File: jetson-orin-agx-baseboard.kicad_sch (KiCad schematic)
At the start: 0 parts

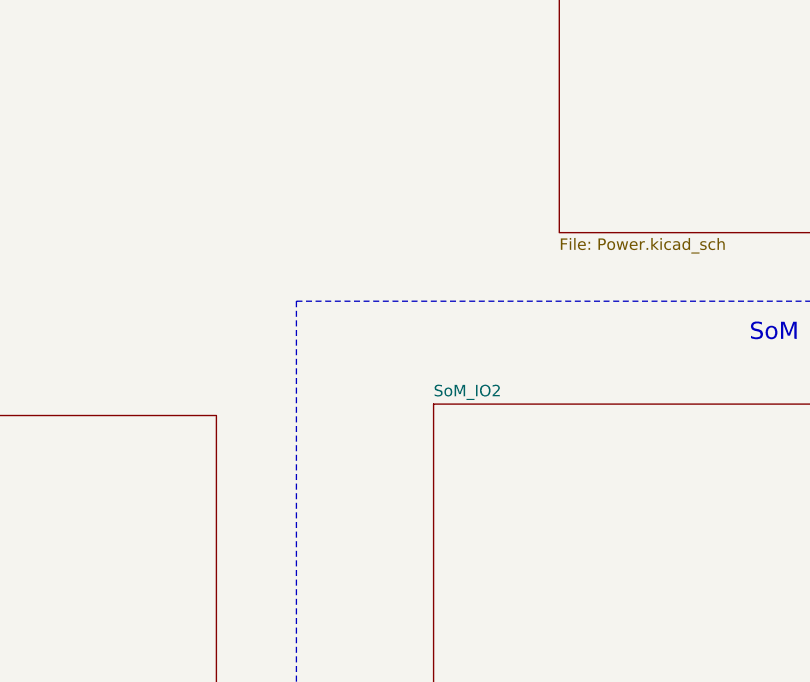
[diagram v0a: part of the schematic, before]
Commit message: [#81782] Add DC section
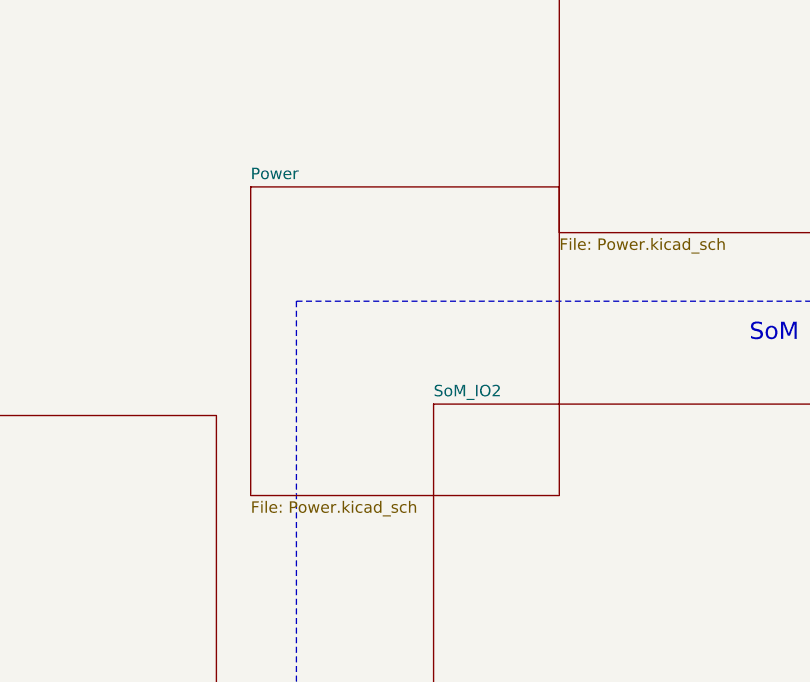
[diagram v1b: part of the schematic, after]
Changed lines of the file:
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@@
+		)
+	)
+	(sheet
+		(at 228.6 119.38)
+		(size 34.29 34.29)
+		(exclude_from_sim no)
+		(in_bom yes)
+		(on_board yes)
+		(dnp no)
+		(fields_autoplaced yes)
+		(stroke
+			(width 0.1524)
+			(type solid)
+		)
+		(fill
+			(color 0 0 0 0.0000)
+		)
+		(property "Sheetname" "Power"
+			(at 228.6 118.6684 0)
+			(effects
+				(font
+					(size 1.27 1.27)
+				)
+				(justify left bottom)
+			)
+		)
+		(property "Sheetfile" "Power.kicad_sch"
+			(at 228.6 154.2546 0)
+			(effects
+				(font
+					(size 1.27 1.27)
+				)
+				(justify left top)
+			)
+		)
+		(instances
+			(project "jetson-orin-agx-baseboard"
+				(path "/f569b0be-0afd-48b7-93ee-28582a4c645c"
+					(page "7")
+				)
+			)
 		)
 	)

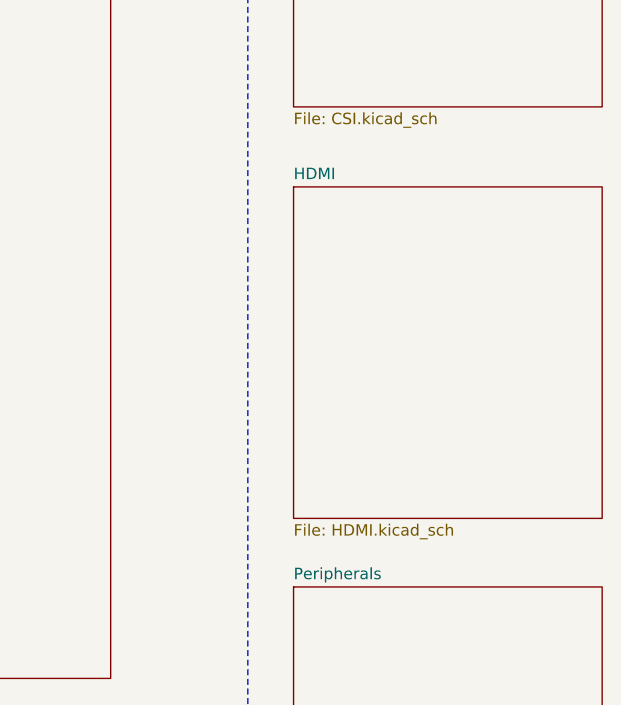
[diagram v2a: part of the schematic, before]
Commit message: [#81970] Add SFP sheet and power section
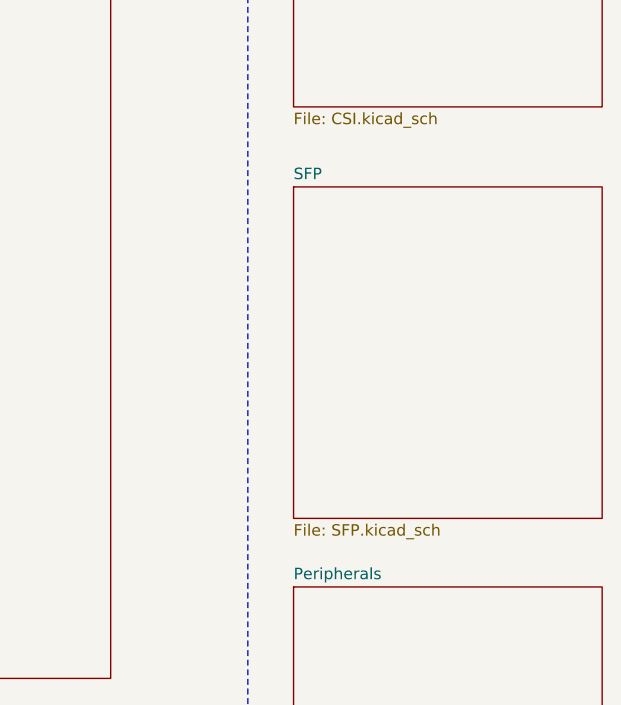
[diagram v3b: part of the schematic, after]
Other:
- sheet HDMI renamed SFP
- sheet SFP: file HDMI.kicad_sch -> SFP.kicad_sch
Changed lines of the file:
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@@
 			(color 0 0 0 0.0000)
 		)
-		(property "Sheetname" "HDMI"
+		(property "Sheetname" "SFP"
 			(at 346.71 235.5084 0)
 			(effects
@@
 			)
 		)
-		(property "Sheetfile" "HDMI.kicad_sch"
+		(property "Sheetfile" "SFP.kicad_sch"
 			(at 346.71 273.6346 0)
 			(effects

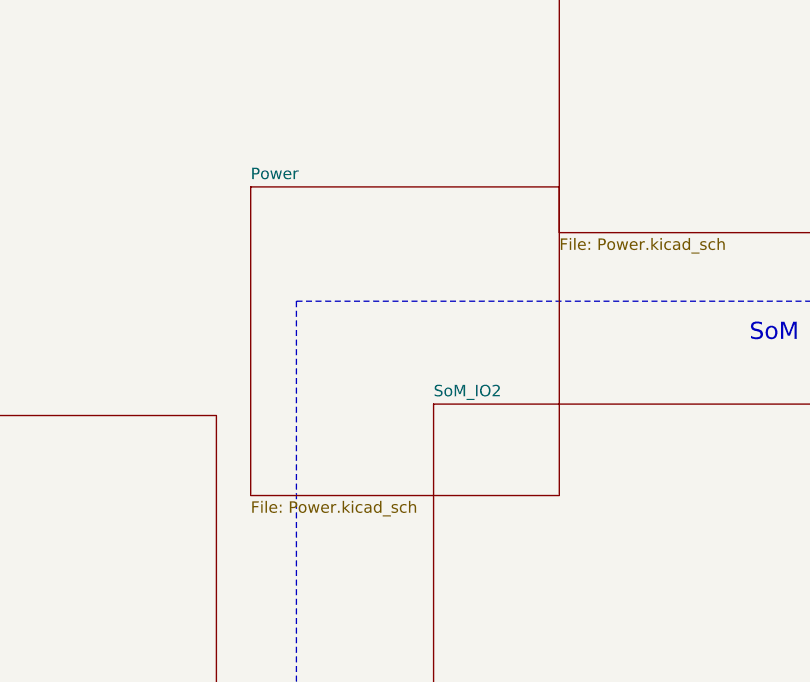
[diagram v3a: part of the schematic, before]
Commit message: [#81970] Finalize connecting SFP+ to SOM
[#82054] Update SoM pins definitions

[#82054] Continue work on I2C

[#82330] Clean up

[#81970] Add SFP sheet and power section

[#82330] Annotation and clean up
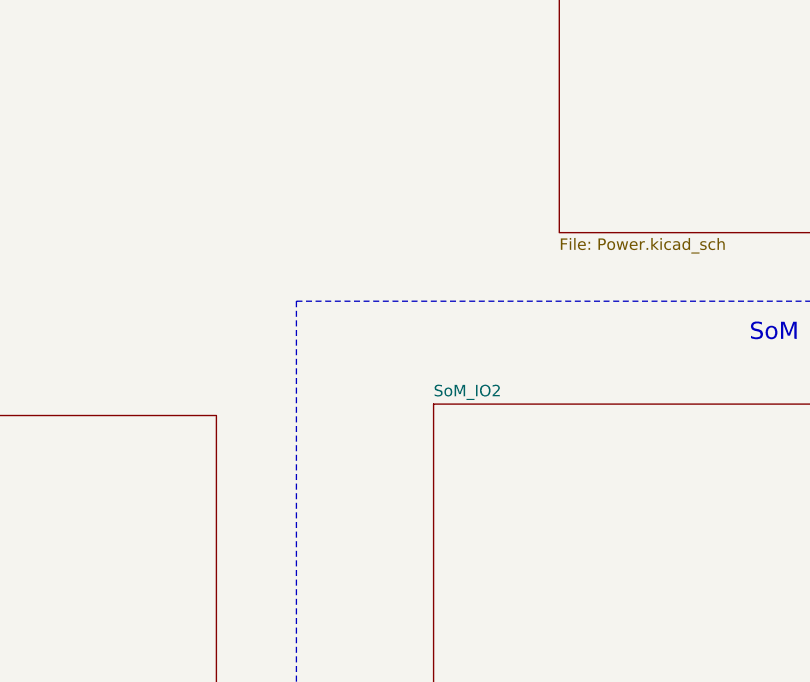
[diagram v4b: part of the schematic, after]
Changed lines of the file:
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@@
-	)
-	(sheet
-		(at 228.6 119.38)
-		(size 34.29 34.29)
-		(exclude_from_sim no)
-		(in_bom yes)
-		(on_board yes)
-		(dnp no)
-		(fields_autoplaced yes)
-		(stroke
-			(width 0.1524)
-			(type solid)
-		)
-		(fill
-			(color 0 0 0 0.0000)
-		)
-		(property "Sheetname" "Power"
-			(at 228.6 118.6684 0)
-			(effects
-				(font
-					(size 1.27 1.27)
-				)
-				(justify left bottom)
-			)
-		)
-		(property "Sheetfile" "Power.kicad_sch"
-			(at 228.6 154.2546 0)
-			(effects
-				(font
-					(size 1.27 1.27)
-				)
-				(justify left top)
-			)
-		)
-		(instances
-			(project "jetson-orin-agx-baseboard"
-				(path "/f569b0be-0afd-48b7-93ee-28582a4c645c"
-					(page "7")
-				)
-			)
-		)
 	)
 	(sheet

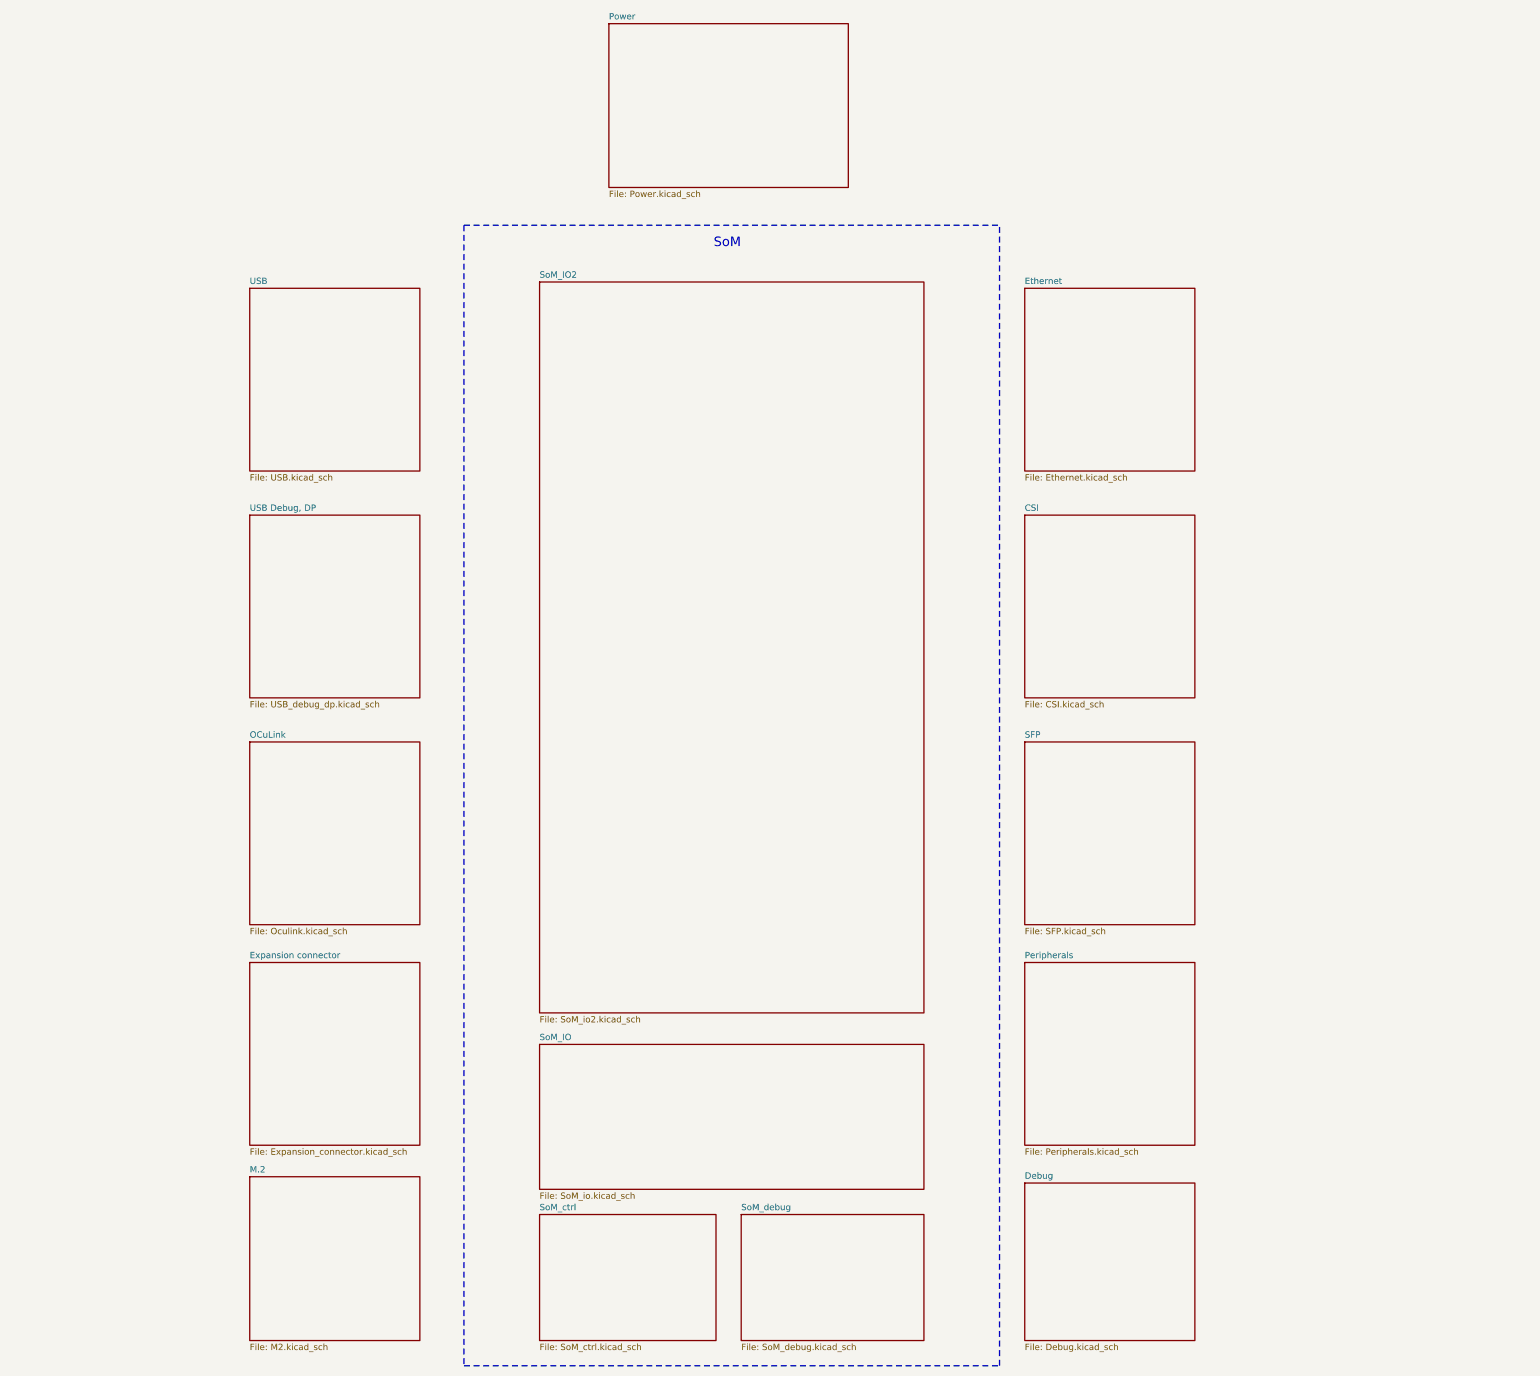
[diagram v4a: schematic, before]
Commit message: [#81970] Reorganise root schematic and place sheet pins
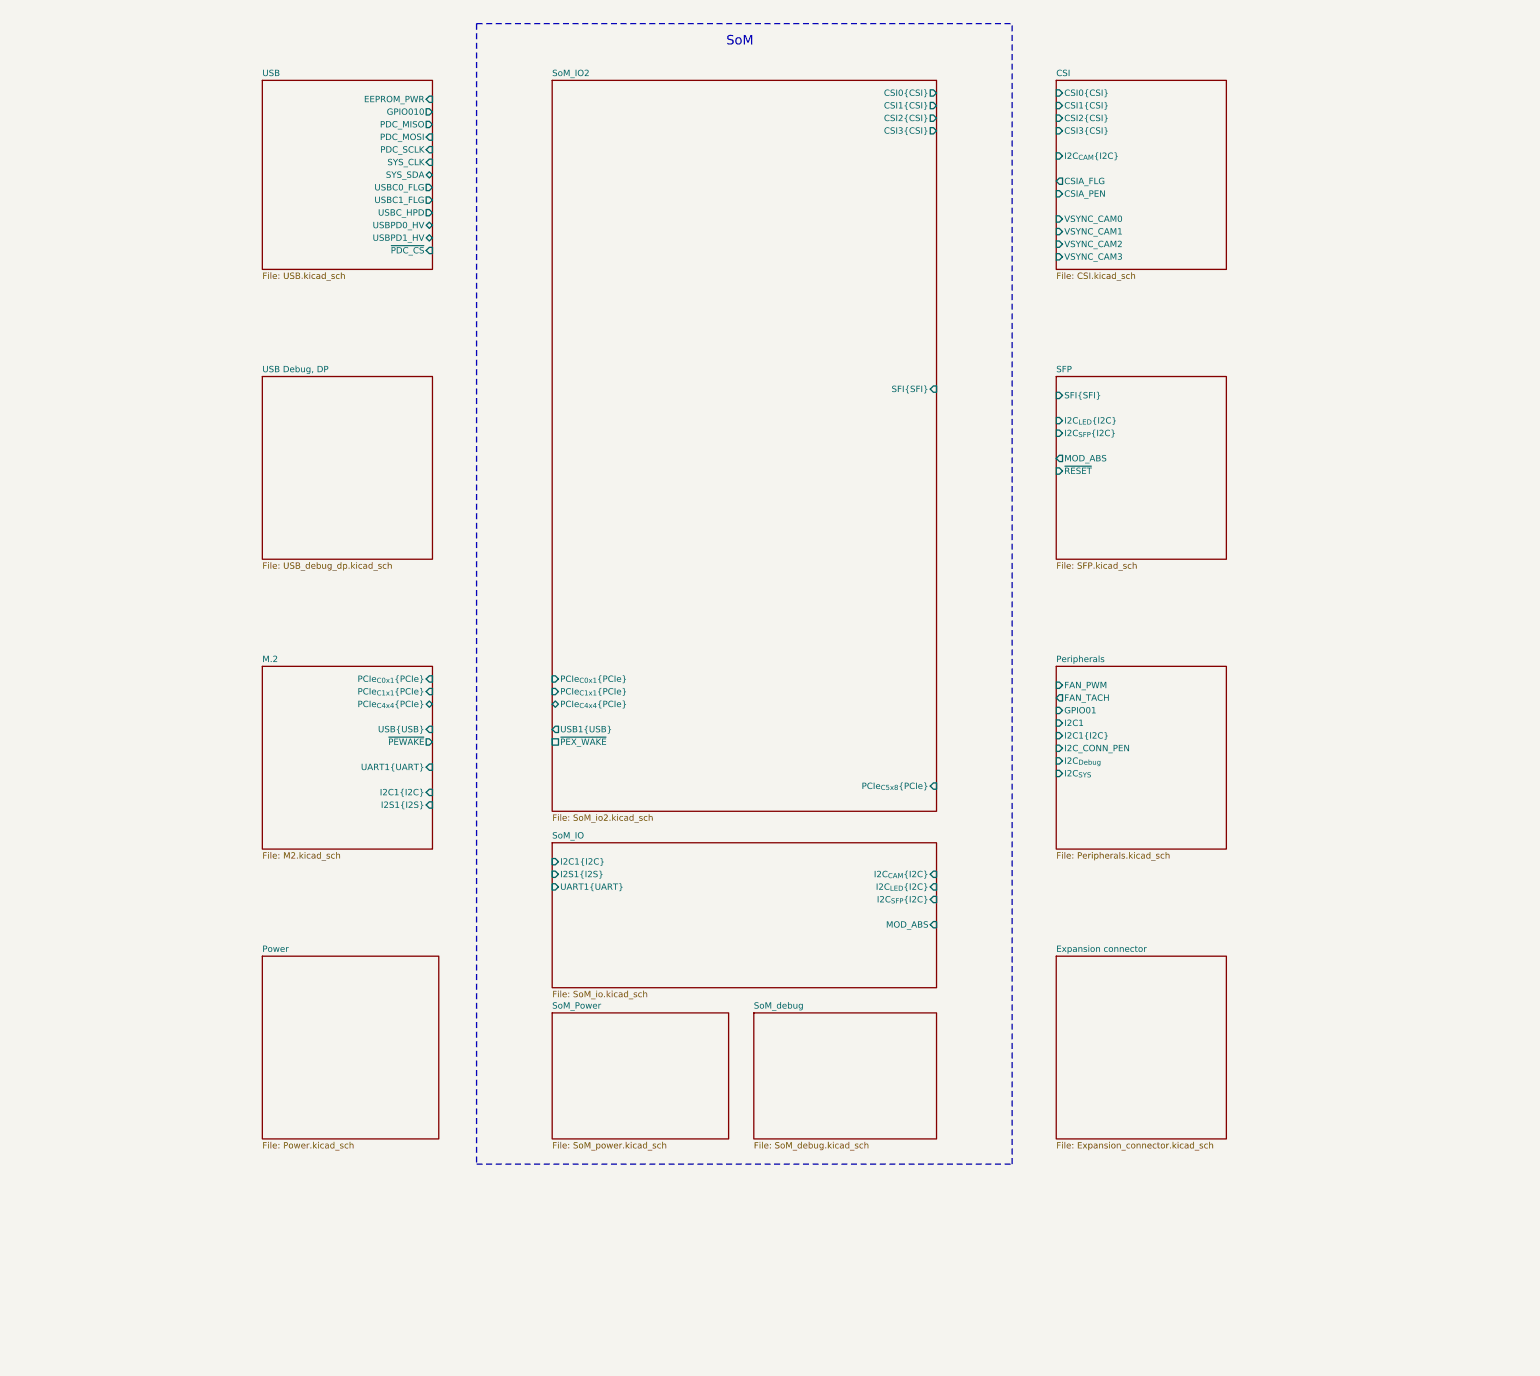
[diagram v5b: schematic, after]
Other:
- sheet SoM_ctrl renamed SoM_Power
- removed sheet Debug
- removed sheet Ethernet
- removed sheet OCuLink
- sheet CSI ports: added CSI0{CSI}, CSI1{CSI}, CSI2{CSI}, CSI3{CSI}, CSIA_FLG, CSIA_PEN, I2C_{CAM}{I2C}, VSYNC_CAM0, VSYNC_CAM1, VSYNC_CAM2, VSYNC_CAM3; removed none
- sheet M.2 ports: added I2C1{I2C}, I2S1{I2S}, PCIe_{C0x1}{PCIe}, PCIe_{C1x1}{PCIe}, PCIe_{C4x4}{PCIe}, UART1{UART}, USB{USB}, ~{PEWAKE}; removed none
- sheet Peripherals ports: added FAN_PWM, FAN_TACH, GPIO01, I2C1, I2C1{I2C}, I2C_CONN_PEN, I2C_{Debug}, I2C_{SYS}; removed none
- sheet SFP ports: added I2C_{LED}{I2C}, I2C_{SFP}{I2C}, MOD_ABS, SFI{SFI}, ~{RESET}; removed none
- sheet SoM_IO ports: added I2C1{I2C}, I2C_{CAM}{I2C}, I2C_{LED}{I2C}, I2C_{SFP}{I2C}, I2S1{I2S}, MOD_ABS, UART1{UART}; removed none
- sheet SoM_IO2 ports: added CSI0{CSI}, CSI1{CSI}, CSI2{CSI}, CSI3{CSI}, PCIe_{C0x1}{PCIe}, PCIe_{C1x1}{PCIe}, PCIe_{C4x4}{PCIe}, PCIe_{C5x8}{PCIe}, SFI{SFI}, USB1{USB}, ~{PEX_WAKE}; removed none
- sheet SoM_Power: file SoM_ctrl.kicad_sch -> SoM_power.kicad_sch
- sheet USB ports: added EEPROM_PWR, GPIO010, PDC_MISO, PDC_MOSI, PDC_SCLK, SYS_CLK, SYS_SDA, USBC0_FLG, USBC1_FLG, USBC_HPD, USBPD0_HV, USBPD1_HV, ~{PDC_CS}; removed none
